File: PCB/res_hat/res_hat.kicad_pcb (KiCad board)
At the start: 2 copper layers, 85 x 56 mm, 55 parts, among them IC1 MCP4725A0T-E_CH, IC2 MCP4725A0T-E_CH, IC3 UCC27324D, J1 Conn_02x20_Odd_Even, J10 Conn_01x02, J11 Jack-DC, J2 Conn_02x04_Odd_Even, J3 Conn_01x03, J4 Conn_01x06, J5 Conn_Coaxial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

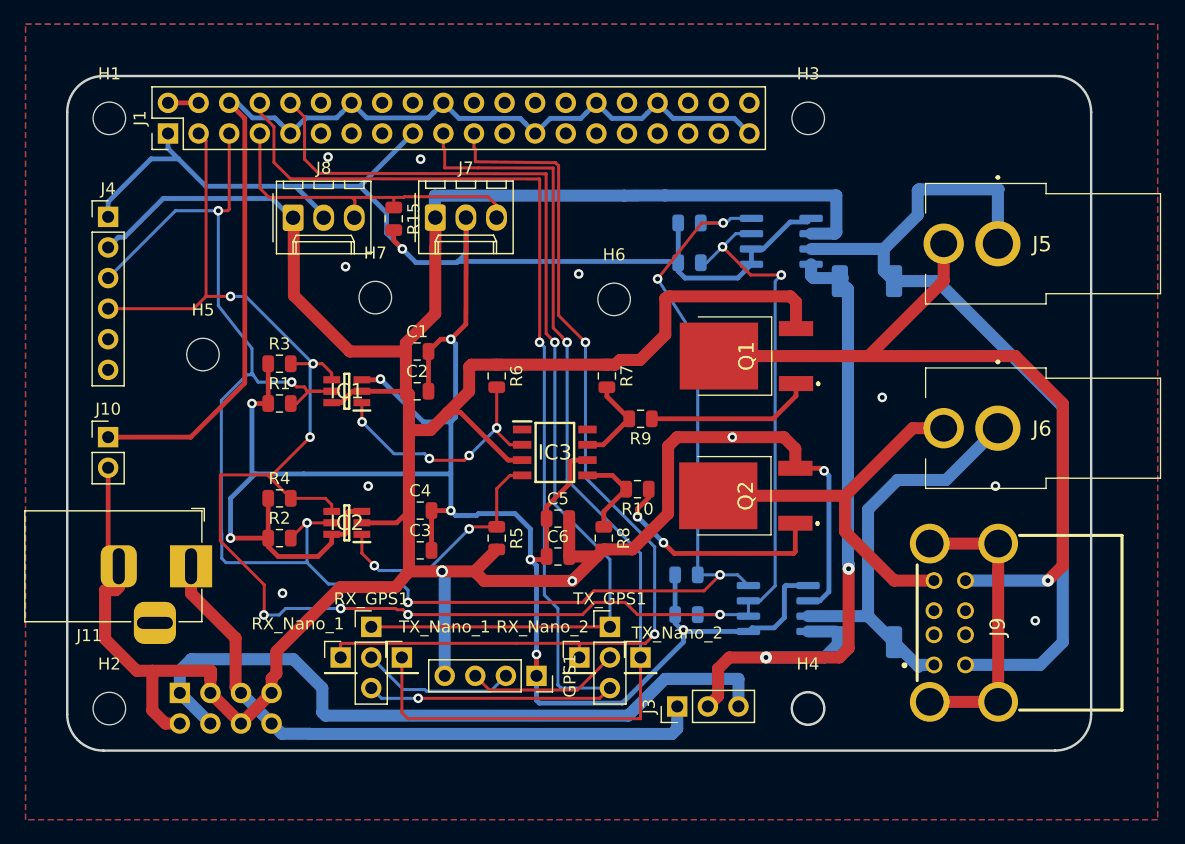
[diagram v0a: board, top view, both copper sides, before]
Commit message: update position off gps and optimise pcb
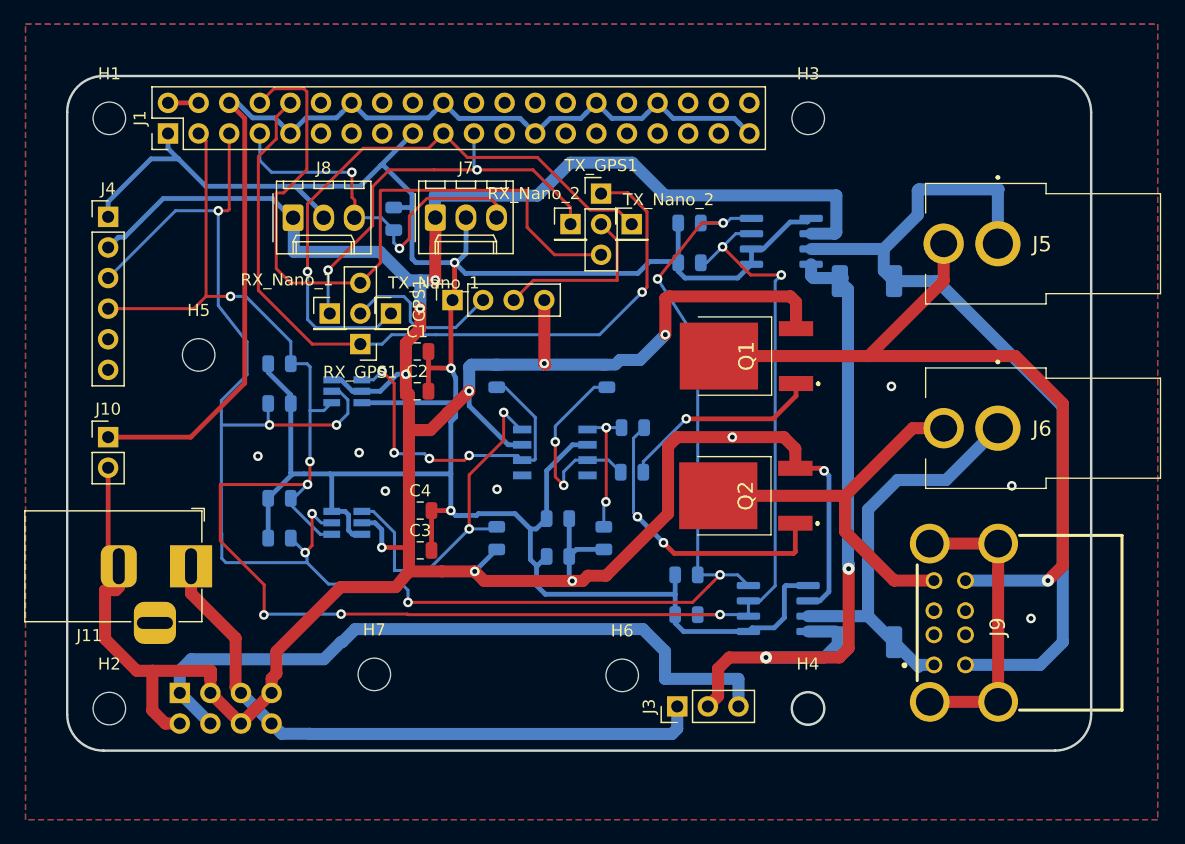
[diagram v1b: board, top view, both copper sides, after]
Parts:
- C5, C6, IC1, IC2, IC3, R1, R10, R15, R2, R3, R4, R5, R6, R7, R8, R9: moved to B.Cu
- moved RX_Nano_2 36.0 mm to (103.7, 110.6)
- moved TX_Nano_2 36.0 mm to (108.7, 110.6)
- moved TX_GPS1 36.0 mm to (106.2, 108.0)
- moved GPS1 32.0 mm to (93.9, 116.9), turned to 90 degrees
- moved H7 31.3 mm to (87.4, 148.0)
- moved H6 31.2 mm to (108.0, 148.0)
- moved RX_Nano_1 28.6 mm to (83.7, 118.0)
- moved TX_Nano_1 28.6 mm to (88.8, 118.0)
- moved RX_GPS1 23.5 mm to (86.2, 120.5), turned to 180 degrees
- moved R10 5.12 mm to (108.8, 127.5)
- moved R9 4.49 mm to (108.8, 131.2)
- moved H5 0.36 mm to (72.8, 121.4)
- turned R1 to 180 degrees
- turned R15 to 90 degrees
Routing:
- net /UART_RX_NanopiM4: track 80.3 -> 34.9 mm
- net /UART_TX: track 95.6 -> 58.8 mm, vias 2 -> 0
- net /UART_TX_NanopiM4: track 85.5 -> 49.7 mm
- net +3V3: track 253.8 -> 226.1 mm, vias 9 -> 3
- net /UART_RX: track 85.3 -> 63.5 mm
- net Net-(IC3-Pad7): track 7.75 -> 17.5 mm, vias 0 -> 2
- net Net-(IC2-Pad1): track 20.6 -> 29.6 mm
- net Net-(IC1-Pad1): track 21.5 -> 29.2 mm
- net /SCL: track 154.1 -> 159.5 mm, vias 7 -> 9
- net Net-(Q2-Pad1): track 19.5 -> 24.7 mm
- net /1-Wire: track 29.1 -> 33.3 mm, vias 0 -> 2
- net Net-(IC3-Pad5): track 7.58 -> 11.2 mm, vias 0 -> 2
- net Net-(Q1-Pad1): track 13.8 -> 16.8 mm, vias 0 -> 1
- net /tx_gps: track 12.8 -> 14.5 mm
- net /SDA: track 157.3 -> 156.1 mm, vias 9 -> 8
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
